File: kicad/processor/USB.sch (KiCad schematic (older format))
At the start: 18 parts, among them Q201 MMBT4401, Q202 MMBT4401, SW201 SWITCH_PUSHBUTTON, SW202 SWITCH_PUSHBUTTON, U201 USB_B_Socket, U202 SP3003-04, U203 CP2102N

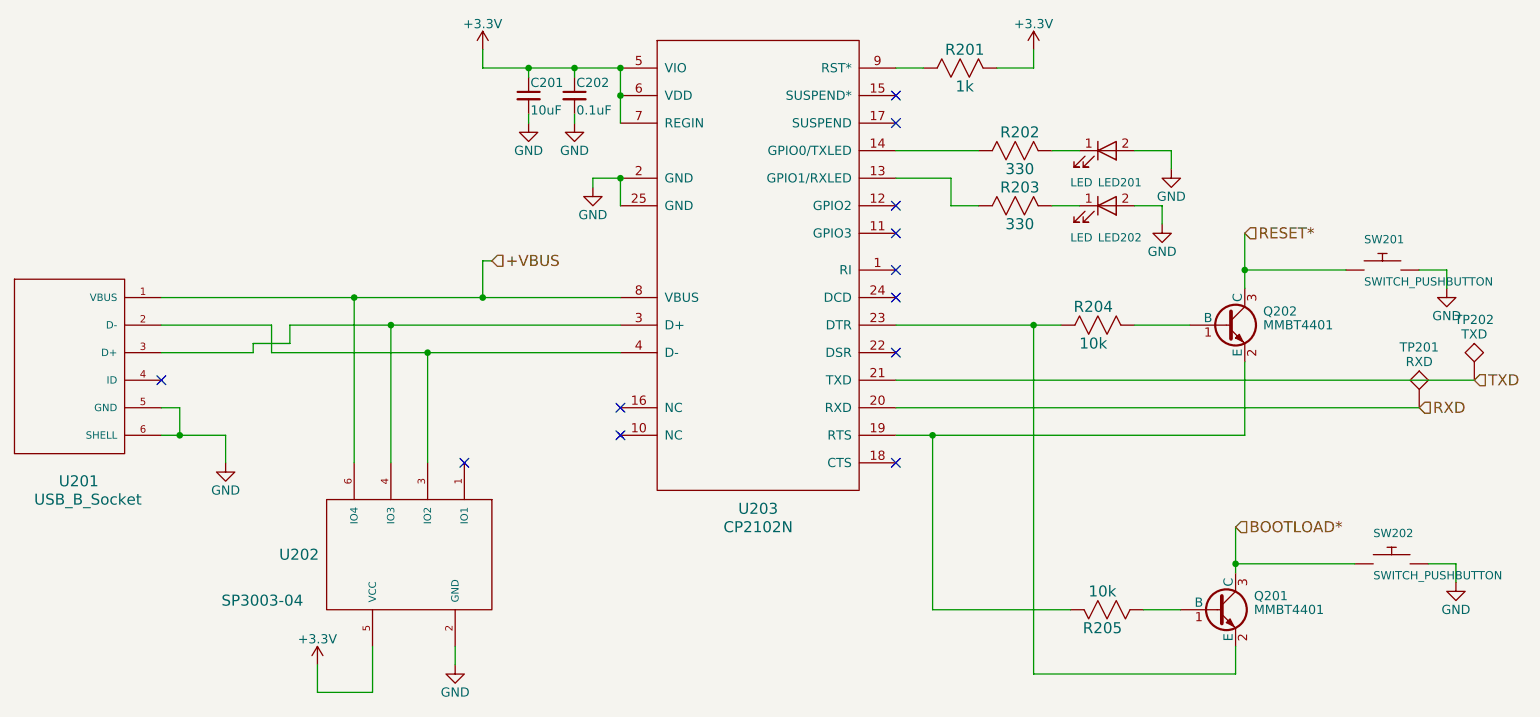
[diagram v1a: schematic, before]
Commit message: Finish split projects, fix ERC, import outline to processor board
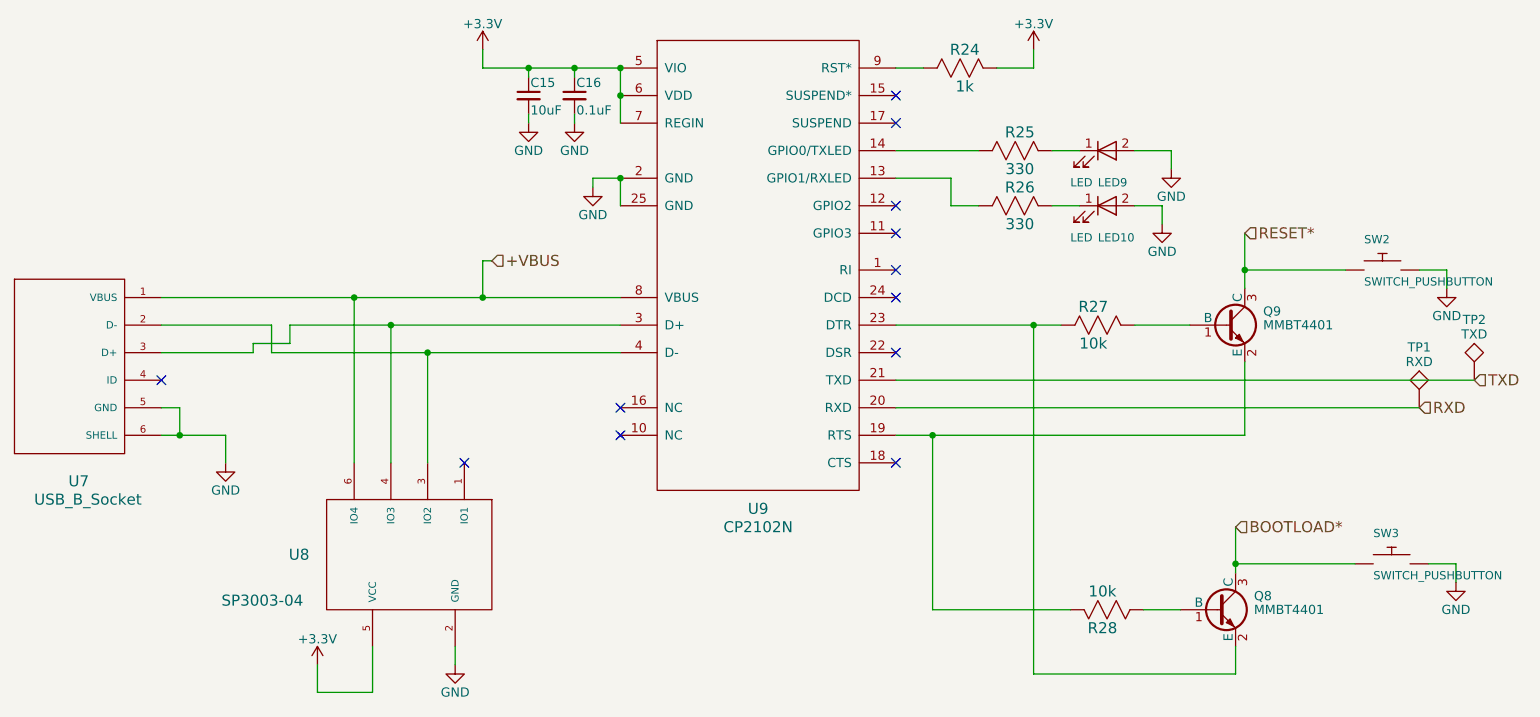
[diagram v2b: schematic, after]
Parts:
- renumbered C201 to C15, C202 to C16, LED202 to LED10, LED201 to LED9, Q201 to Q8, Q202 to Q9, R201 to R24, R202 to R25, R203 to R26, R204 to R27, R205 to R28, SW201 to SW2, SW202 to SW3, TP201 to TP1, TP202 to TP2, U201 to U7, U202 to U8, U203 to U9

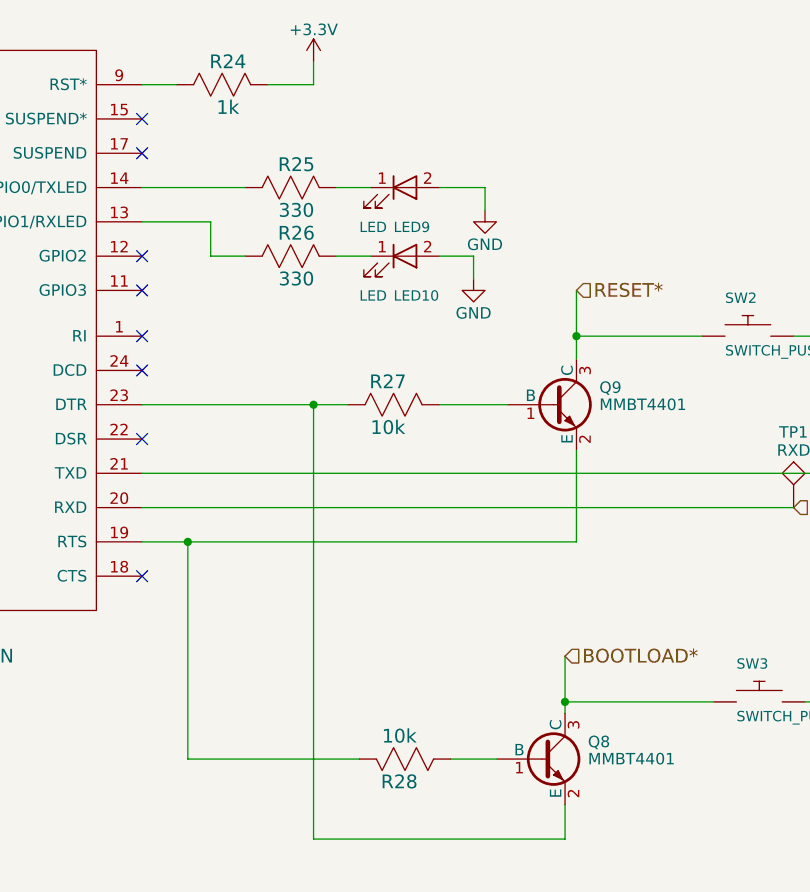
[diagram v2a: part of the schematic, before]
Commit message: Logic board standalone about done, changed to 0603 resistors and 0805 caps
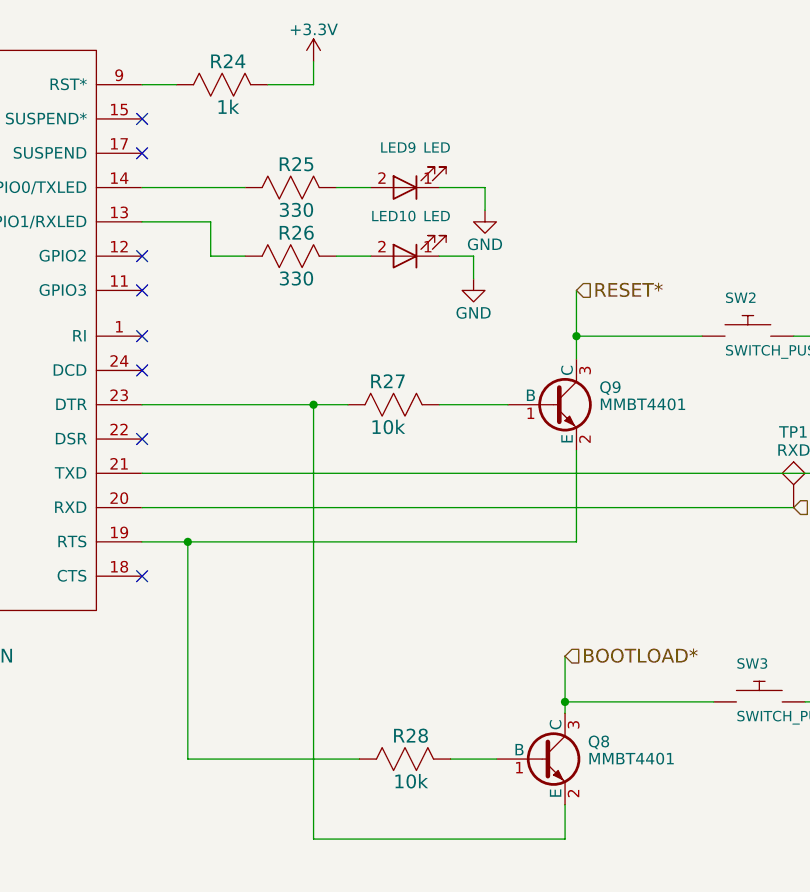
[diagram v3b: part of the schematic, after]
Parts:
- C15: footprint paddle:SMD_1206 -> paddle:SMD_0805
- R24, R25, R26: footprint paddle:R_0805 -> paddle:R_0603
- R27, R28: footprint paddle:SMD_0805 -> paddle:R_0603
- U9: footprint paddle:QFN-24-1EP_4x4mm_Pitch0.5mm -> paddle:QFP24
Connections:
- net GND: now also LED10.1 (K), LED9.1 (K); no longer LED10.2 (A), LED9.2 (A)
- net at R26.2: now also LED10.2 (A); no longer LED10.1 (K)
- net at R25.2: now also LED9.2 (A); no longer LED9.1 (K)
- net at Q9.2 (E), U9.19 (RTS): now also R28.1; no longer R28.2
- net at Q8.1 (B): now also R28.2; no longer R28.1
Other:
- moved on the sheet: LED10, LED9
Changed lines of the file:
@@
 F 0 "U9" H 5400 2000 60  0000 C CNN
 F 1 "CP2102N" H 5400 1900 60  0000 C CNN
-F 2 "paddle:QFN-24-1EP_4x4mm_Pitch0.5mm" H 5450 2350 60  0001 C CNN
+F 2 "paddle:QFP24" H 5450 2350 60  0001 C CNN
 F 3 "" H 5450 2350 60  0001 C CNN
 	1    5400 3300
@@
 F 0 "C15" H 4160 2420 50  0000 L CNN
 F 1 "10uF" H 4160 2270 50  0000 L CNN
-F 2 "paddle:SMD_1206" H 4150 2350 50  0001 C CNN
+F 2 "paddle:SMD_0805" H 4150 2350 50  0001 C CNN
 F 3 "" H 4150 2350 50  0001 C CNN
 	1    4150 2350
@@
 F 0 "R28" H 7325 5250 60  0000 C CNN
 F 1 "10k" H 7325 5050 60  0000 C CNN
-F 2 "paddle:SMD_0805" H 7300 4800 60  0001 C CNN
+F 2 "paddle:R_0603" H 7300 4800 60  0001 C CNN
 F 3 "" H 7325 5250 60  0000 C CNN
 	1    7300 5150
-	-1   0    0    1
+	1    0    0    -1
 $EndComp
 $Comp
@@
 F 0 "R27" H 7275 3700 60  0000 C CNN
 F 1 "10k" H 7275 3500 60  0000 C CNN
-F 2 "paddle:SMD_0805" H 7250 3250 60  0001 C CNN
+F 2 "paddle:R_0603" H 7250 3250 60  0001 C CNN
 F 3 "" H 7275 3700 60  0000 C CNN
 	1    7250 3600
@@
 F 3 "" V 7250 2950 60  0001 C CNN
 	1    7300 2950
-	1    0    0    -1
+	-1   0    0    1
 $EndComp
 $Comp
@@
 F 0 "R26" H 6825 3050 60  0000 C CNN
 F 1 "330" H 6825 2850 60  0000 C CNN
-F 2 "paddle:R_0805" H 6800 2600 60  0001 C CNN
+F 2 "paddle:R_0603" H 6800 2600 60  0001 C CNN
 F 3 "" H 6825 3050 60  0000 C CNN
 	1    6800 2950
@@
 F 3 "" V 7250 2650 60  0001 C CNN
 	1    7300 2650
-	1    0    0    -1
+	-1   0    0    1
 $EndComp
 $Comp
@@
 F 0 "R25" H 6825 2750 60  0000 C CNN
 F 1 "330" H 6825 2550 60  0000 C CNN
-F 2 "paddle:R_0805" H 6800 2300 60  0001 C CNN
+F 2 "paddle:R_0603" H 6800 2300 60  0001 C CNN
 F 3 "" H 6825 2750 60  0000 C CNN
 	1    6800 2650
@@
 F 0 "R24" H 6525 2300 60  0000 C CNN
 F 1 "1k" H 6525 2100 60  0000 C CNN
-F 2 "paddle:R_0805" H 6500 1850 60  0001 C CNN
+F 2 "paddle:R_0603" H 6500 1850 60  0001 C CNN
 F 3 "" H 6525 2300 60  0000 C CNN
 	1    6500 2200

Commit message: start processor layout - footprint fixes
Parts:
- U9: footprint paddle:QFP24 -> paddle:QFP_24
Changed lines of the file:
@@
 F 0 "U9" H 5400 2000 60  0000 C CNN
 F 1 "CP2102N" H 5400 1900 60  0000 C CNN
-F 2 "paddle:QFP24" H 5450 2350 60  0001 C CNN
+F 2 "paddle:QFP_24" H 5450 2350 60  0001 C CNN
 F 3 "" H 5450 2350 60  0001 C CNN
 	1    5400 3300

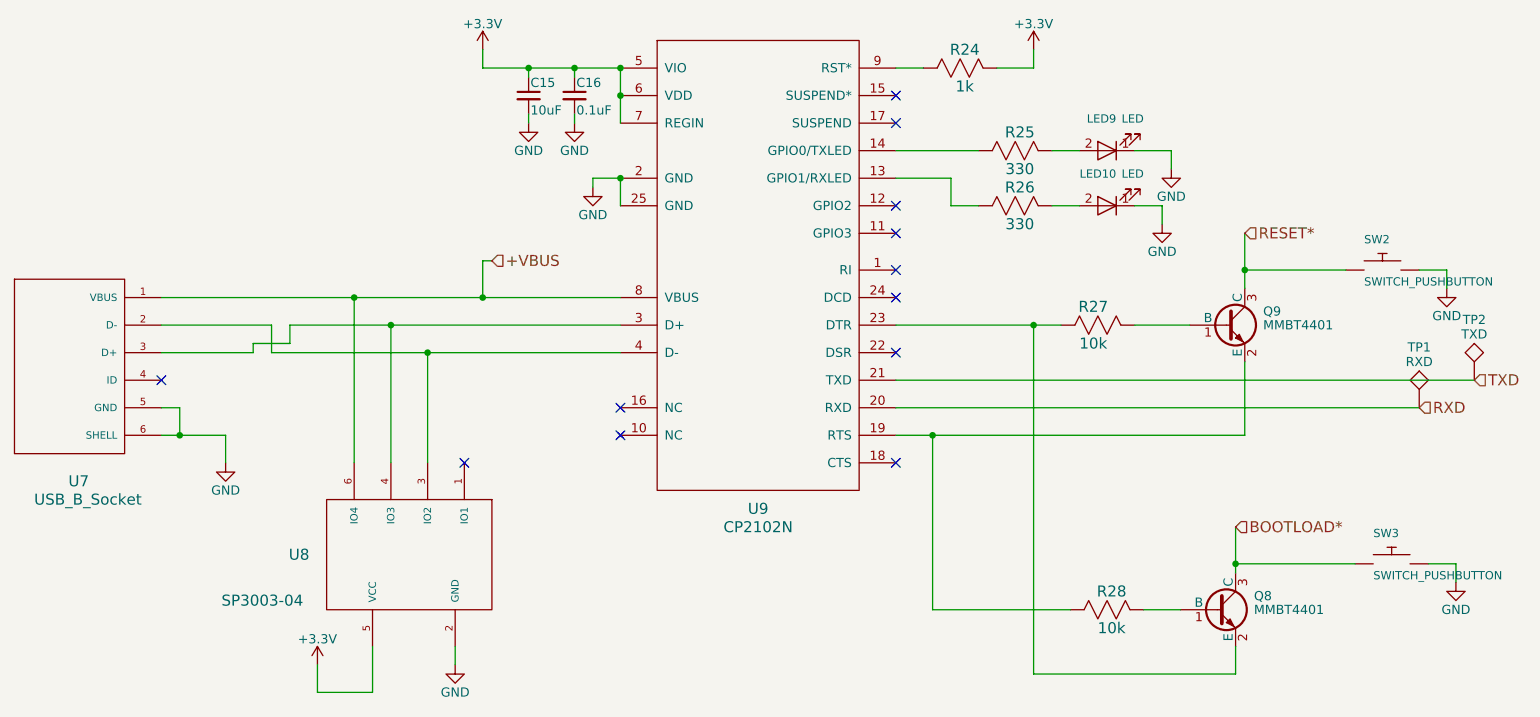
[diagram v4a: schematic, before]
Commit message: First cut layout power supply, fix netclasses, footprint for connector
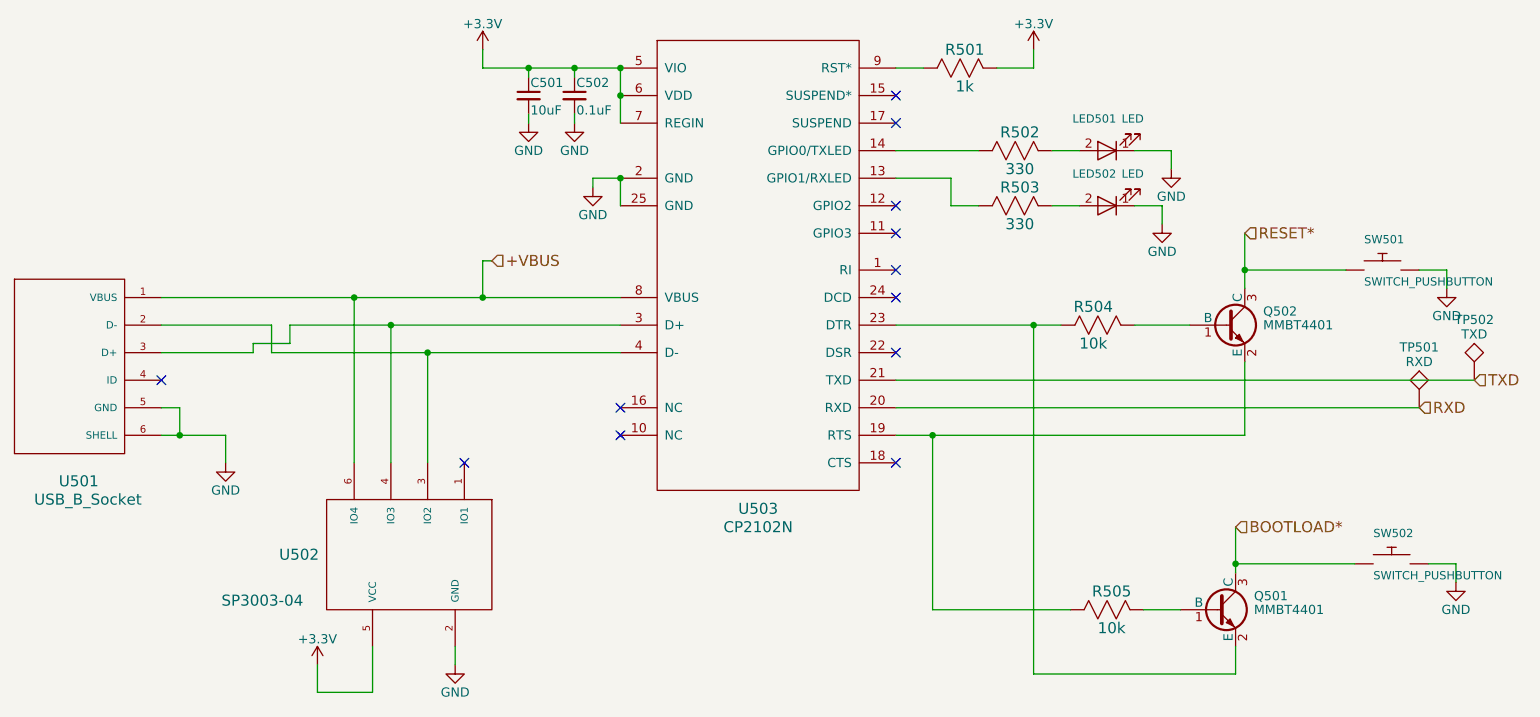
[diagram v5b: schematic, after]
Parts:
- renumbered C15 to C501, C16 to C502, LED9 to LED501, LED10 to LED502, Q8 to Q501, Q9 to Q502, R24 to R501, R25 to R502, R26 to R503, R27 to R504, R28 to R505, SW2 to SW501, SW3 to SW502, TP1 to TP501, TP2 to TP502, U7 to U501, U8 to U502, U9 to U503
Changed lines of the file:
@@
 $EndDescr
 $Comp
-L CP2104 U9
+L CP2104 U503
 U 1 1 59C7A894
 P 5400 3300
-F 0 "U9" H 5400 2000 60  0000 C CNN
+F 0 "U503" H 5400 2000 60  0000 C CNN
 F 1 "CP2102N" H 5400 1900 60  0000 C CNN
 F 2 "paddle:QFP_24" H 5450 2350 60  0001 C CNN
@@
 $EndComp
 $Comp
-L C_Small C16
+L C_Small C502
 U 1 1 59C7A8A4
 P 4400 2350
-F 0 "C16" H 4410 2420 50  0000 L CNN
+F 0 "C502" H 4410 2420 50  0000 L CNN
 F 1 "0.1uF" H 4410 2270 50  0000 L CNN
 F 2 "paddle:SMD_0805" H 4400 2350 50  0001 C CNN
@@
 $EndComp
 $Comp
-L C_Small C15
+L C_Small C501
 U 1 1 59C7A8B1
 P 4150 2350
-F 0 "C15" H 4160 2420 50  0000 L CNN
+F 0 "C501" H 4160 2420 50  0000 L CNN
 F 1 "10uF" H 4160 2270 50  0000 L CNN
 F 2 "paddle:SMD_0805" H 4150 2350 50  0001 C CNN
@@
 NoConn ~ 4650 4200
 $Comp
-L NPN_BEC_SOT-23 Q8
+L NPN_BEC_SOT-23 Q501
 U 1 1 59C7A8C7
 P 7900 5150
-F 0 "Q8" H 8100 5225 50  0000 L CNN
+F 0 "Q501" H 8100 5225 50  0000 L CNN
 F 1 "MMBT4401" H 8100 5150 50  0000 L CNN
 F 2 "paddle:SOT-23" H 8100 5075 50  0001 L CIN
@@
 $EndComp
 $Comp
-L NPN_BEC_SOT-23 Q9
+L NPN_BEC_SOT-23 Q502
 U 1 1 59C7A8CE
 P 7950 3600
-F 0 "Q9" H 8150 3675 50  0000 L CNN
+F 0 "Q502" H 8150 3675 50  0000 L CNN
 F 1 "MMBT4401" H 8150 3600 50  0000 L CNN
 F 2 "paddle:SOT-23" H 8150 3525 50  0001 L CIN
@@
 $EndComp
 $Comp
-L R_US R28
+L R_US R505
 U 1 1 59C7A8D5
 P 7300 5150
-F 0 "R28" H 7325 5250 60  0000 C CNN
+F 0 "R505" H 7325 5250 60  0000 C CNN
 F 1 "10k" H 7325 5050 60  0000 C CNN
 F 2 "paddle:R_0603" H 7300 4800 60  0001 C CNN
@@
 $EndComp
 $Comp
-L R_US R27
+L R_US R504
 U 1 1 59C7A8DC
 P 7250 3600
-F 0 "R27" H 7275 3700 60  0000 C CNN
+F 0 "R504" H 7275 3700 60  0000 C CNN
 F 1 "10k" H 7275 3500 60  0000 C CNN
 F 2 "paddle:R_0603" H 7250 3250 60  0001 C CNN
@@
 +VBUS
 $Comp
-L LED LED10
+L LED LED502
 U 1 1 59C748D3
 P 7300 2950
-F 0 "LED10" H 7250 2750 45  0000 L BNN
+F 0 "LED502" H 7250 2750 45  0000 L BNN
 F 1 "LED" H 7100 2750 45  0000 L BNN
 F 2 "paddle:SMD_D_0805" H 7100 2980 20  0001 C CNN
@@
 $EndComp
 $Comp
-L R_US R26
+L R_US R503
 U 1 1 59C74976
 P 6800 2950
-F 0 "R26" H 6825 3050 60  0000 C CNN
+F 0 "R503" H 6825 3050 60  0000 C CNN
 F 1 "330" H 6825 2850 60  0000 C CNN
 F 2 "paddle:R_0603" H 6800 2600 60  0001 C CNN
@@
 $EndComp
 $Comp
-L LED LED9
+L LED LED501
 U 1 1 59C74B26
 P 7300 2650
-F 0 "LED9" H 7250 2450 45  0000 L BNN
+F 0 "LED501" H 7250 2450 45  0000 L BNN
 F 1 "LED" H 7100 2450 45  0000 L BNN
 F 2 "paddle:SMD_D_0805" H 7100 2680 20  0001 C CNN
@@
 $EndComp
 $Comp
-L R_US R25
+L R_US R502
 U 1 1 59C74B2C
 P 6800 2650
-F 0 "R25" H 6825 2750 60  0000 C CNN
+F 0 "R502" H 6825 2750 60  0000 C CNN
 F 1 "330" H 6825 2550 60  0000 C CNN
 F 2 "paddle:R_0603" H 6800 2300 60  0001 C CNN
@@
 $EndComp
 $Comp
-L R_US R24
+L R_US R501
 U 1 1 59C74D40
 P 6500 2200
-F 0 "R24" H 6525 2300 60  0000 C CNN
+F 0 "R501" H 6525 2300 60  0000 C CNN
 F 1 "1k" H 6525 2100 60  0000 C CNN
 F 2 "paddle:R_0603" H 6500 1850 60  0001 C CNN
@@
 $EndComp
 $Comp
-L USB_B_Socket U7
+L USB_B_Socket U501
 U 1 1 59CE57D2
 P 1750 3800
-F 0 "U7" H 1700 3150 60  0000 C CNN
+F 0 "U501" H 1700 3150 60  0000 C CNN
 F 1 "USB_B_Socket" H 1750 3050 60  0000 C CNN
 F 2 "paddle:USB_micro_B_FCI_10104110" H 1700 3150 60  0001 C CNN
@@
 NoConn ~ 2150 3900
 $Comp
-L SP3003-04 U8
+L SP3003-04 U502
 U 1 1 59CE7D75
 P 3500 4850
-F 0 "U8" V 3500 4250 60  0000 C CNN
+F 0 "U502" V 3500 4250 60  0000 C CNN
 F 1 "SP3003-04" V 3750 4050 60  0000 C CNN
 F 2 "paddle:SMD_SC70-6" H 3500 3900 60  0001 C CNN
@@
 $EndComp
 $Comp
-L TEST TP2
+L TEST TP502
 U 1 1 59D07069
 P 9300 3900
-F 0 "TP2" H 9300 4200 50  0000 C BNN
+F 0 "TP502" H 9300 4200 50  0000 C BNN
 F 1 "TXD" H 9300 4150 50  0000 C CNN
 F 2 "paddle:tp_th_1mm" H 9300 3900 50  0001 C CNN
@@
 $EndComp
 $Comp
-L TEST TP1
+L TEST TP501
 U 1 1 59D07090
 P 9000 4050
-F 0 "TP1" H 9000 4350 50  0000 C BNN
+F 0 "TP501" H 9000 4350 50  0000 C BNN
 F 1 "RXD" H 9000 4300 50  0000 C CNN
 F 2 "paddle:tp_th_1mm" H 9000 4050 50  0001 C CNN
@@
 AR Path="/59C7A5C1/59D20095" Ref="SW?"  Part="1"
 AR Path="/59FE1414/59FE3441/59D20095" Ref="SW?"  Part="1"
-AR Path="/59FFAD44/59D20095" Ref="SW2"  Part="1"
-F 0 "SW2" H 8700 3440 45  0000 L BNN
+AR Path="/59FFAD44/59D20095" Ref="SW501"  Part="1"
+F 0 "SW501" H 8700 3440 45  0000 L BNN
 F 1 "SWITCH_PUSHBUTTON" H 8700 3210 45  0000 L BNN
 F 2 "paddle:SW_KMR7" H 9100 3500 20  0001 C CNN
@@
 AR Path="/59C7A5C1/59D200ED" Ref="SW?"  Part="1"
 AR Path="/59FE1414/59FE3441/59D200ED" Ref="SW?"  Part="1"
-AR Path="/59FFAD44/59D200ED" Ref="SW3"  Part="1"
-F 0 "SW3" H 8750 5040 45  0000 L BNN
+AR Path="/59FFAD44/59D200ED" Ref="SW502"  Part="1"
+F 0 "SW502" H 8750 5040 45  0000 L BNN
 F 1 "SWITCH_PUSHBUTTON" H 8750 4810 45  0000 L BNN
 F 2 "paddle:SW_KMR7" H 9150 5100 20  0001 C CNN
